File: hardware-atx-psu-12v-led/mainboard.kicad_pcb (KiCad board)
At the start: 2 copper layers, 98 x 103 mm, 100 parts, among them J1 ATX-24, J11 LED, J12 LED, J13 LED, J14 LED, J15 LED, J16 LED, J17 LED, J18 LED, J19 LED, J2 ATX, J20 LED, J21 LED, J22 LED, J23 LED, J24 LED, J25 LED, J26 LED, J27 LED, J28 LED, J29 LED, J3 PA11, J30 LED, J31 LED, J32 LED, J33 LED, J34 LED, J35 LED, J36 LED, J37 LED, J38 LED, J39 LED, J4 PA12, J40 LED, J41 LED, J42 ATX, J43 ATX, J44 ATX, J45 ATX, J5 LED, J6 USB_C_Receptacle_USB2.0, J7 PAGM, J8 PA15, SW1 Download, U1 CH32V305RBT6, U2 AMS1117, Y2 8MHz

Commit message: Tweak holes on power connector
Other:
- board text added: "cnhardware xmastree mainboard rev B"
- board text removed: "cnhardware xmastree mainboard rev A"
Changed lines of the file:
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@@
 			(drillshape 0)
 			(scaleselection 1)
-			(outputdirectory "mainboard-revA/")
+			(outputdirectory "mainboard-revB/")
 		)
 	)
@@
 			(at 0 0.6)
 			(size 2.7 3.3)
-			(drill 1.4)
+			(drill 1.61)
 			(layers "*.Cu" "*.Mask")
 			(remove_unused_layers no)
@@
 			(at 4.2 0.6)
 			(size 2.7 3.3)
-			(drill 1.4)
+			(drill 1.6)
 			(layers "*.Cu" "*.Mask")
 			(remove_unused_layers no)
@@
 			(at 8.4 0.6)
 			(size 2.7 3.3)
-			(drill 1.4)
+			(drill 1.6)
 			(layers "*.Cu" "*.Mask")
 			(remove_unused_layers no)
@@
 			(at 12.6 0.6)
 			(size 2.7 3.3)
-			(drill 1.4)
+			(drill 1.61)
 			(layers "*.Cu" "*.Mask")
 			(remove_unused_layers no)
@@
 			(at 0 4.9)
 			(size 2.7 3.3)
-			(drill 1.4)
+			(drill 1.61)
 			(layers "*.Cu" "*.Mask")
 			(remove_unused_layers no)
@@
 			(at 4.2 4.9)
 			(size 2.7 3.3)
-			(drill 1.4)
+			(drill 1.61)
 			(layers "*.Cu" "*.Mask")
 			(remove_unused_layers no)
@@
 			(at 8.4 4.9)
 			(size 2.7 3.3)
-			(drill 1.4)
+			(drill 1.61)
 			(layers "*.Cu" "*.Mask")
 			(remove_unused_layers no)
@@
 			(at 12.6 4.9)
 			(size 2.7 3.3)
-			(drill 1.4)
+			(drill 1.61)
 			(layers "*.Cu" "*.Mask")
 			(remove_unused_layers no)
@@
 			(at 0 0.6 270)
 			(size 2.7 3.3)
-			(drill 1.4)
+			(drill 1.61)
 			(layers "*.Cu" "*.Mask")
 			(remove_unused_layers no)
@@
 			(at 4.2 0.6 270)
 			(size 2.7 3.3)
-			(drill 1.4)
+			(drill 1.6)
 			(layers "*.Cu" "*.Mask")
 			(remove_unused_layers no)
@@
 			(at 8.4 0.6 270)
 			(size 2.7 3.3)
-			(drill 1.4)
+			(drill 1.6)
 			(layers "*.Cu" "*.Mask")
 			(remove_unused_layers no)
@@
 			(at 12.6 0.6 270)
 			(size 2.7 3.3)
-			(drill 1.4)
+			(drill 1.61)
 			(layers "*.Cu" "*.Mask")
 			(remove_unused_layers no)
@@
 			(at 0 4.9 270)
 			(size 2.7 3.3)
-			(drill 1.4)
+			(drill 1.61)
 			(layers "*.Cu" "*.Mask")
 			(remove_unused_layers no)
@@
 			(at 4.2 4.9 270)
 			(size 2.7 3.3)
-			(drill 1.4)
+			(drill 1.61)
 			(layers "*.Cu" "*.Mask")
 			(remove_unused_layers no)
@@
 			(at 8.4 4.9 270)
 			(size 2.7 3.3)
-			(drill 1.4)
+			(drill 1.61)
 			(layers "*.Cu" "*.Mask")
 			(remove_unused_layers no)
@@
 			(at 12.6 4.9 270)
 			(size 2.7 3.3)
-			(drill 1.4)
+			(drill 1.61)
 			(layers "*.Cu" "*.Mask")
 			(remove_unused_layers no)
@@
 			(at 0 0.6 270)
 			(size 2.7 3.3)
-			(drill 1.4)
+			(drill 1.61)
 			(layers "*.Cu" "*.Mask")
 			(remove_unused_layers no)
@@
 			(at 4.2 0.6 270)
 			(size 2.7 3.3)
-			(drill 1.4)
+			(drill 1.6)
 			(layers "*.Cu" "*.Mask")
 			(remove_unused_layers no)
@@
 			(at 8.4 0.6 270)
 			(size 2.7 3.3)
-			(drill 1.4)
+			(drill 1.6)
 			(layers "*.Cu" "*.Mask")
 			(remove_unused_layers no)
@@
 			(at 12.6 0.6 270)
 			(size 2.7 3.3)
-			(drill 1.4)
+			(drill 1.61)
 			(layers "*.Cu" "*.Mask")
 			(remove_unused_layers no)
@@
 			(at 0 4.9 270)
 			(size 2.7 3.3)
-			(drill 1.4)
+			(drill 1.61)
 			(layers "*.Cu" "*.Mask")
 			(remove_unused_layers no)
@@
 			(at 4.2 4.9 270)
 			(size 2.7 3.3)
-			(drill 1.4)
+			(drill 1.61)
 			(layers "*.Cu" "*.Mask")
 			(remove_unused_layers no)
@@
 			(at 8.4 4.9 270)
 			(size 2.7 3.3)
-			(drill 1.4)
+			(drill 1.61)
 			(layers "*.Cu" "*.Mask")
 			(remove_unused_layers no)
@@
 			(at 12.6 4.9 270)
 			(size 2.7 3.3)
-			(drill 1.4)
+			(drill 1.61)
 			(layers "*.Cu" "*.Mask")
 			(remove_unused_layers no)
@@
 			(at 0 0.6 270)
 			(size 2.7 3.3)
-			(drill 1.4)
+			(drill 1.61)
 			(layers "*.Cu" "*.Mask")
 			(remove_unused_layers no)
@@
 			(at 4.2 0.6 270)
 			(size 2.7 3.3)
-			(drill 1.4)
+			(drill 1.6)
 			(layers "*.Cu" "*.Mask")
 			(remove_unused_layers no)
@@
 			(at 8.4 0.6 270)
 			(size 2.7 3.3)
-			(drill 1.4)
+			(drill 1.6)
 			(layers "*.Cu" "*.Mask")
 			(remove_unused_layers no)
@@
 			(at 12.6 0.6 270)
 			(size 2.7 3.3)
-			(drill 1.4)
+			(drill 1.61)
 			(layers "*.Cu" "*.Mask")
 			(remove_unused_layers no)
@@
 			(at 0 4.9 270)
 			(size 2.7 3.3)
-			(drill 1.4)
+			(drill 1.61)
 			(layers "*.Cu" "*.Mask")
 			(remove_unused_layers no)
@@
 			(at 4.2 4.9 270)
 			(size 2.7 3.3)
-			(drill 1.4)
+			(drill 1.61)
 			(layers "*.Cu" "*.Mask")
 			(remove_unused_layers no)
@@
 			(at 8.4 4.9 270)
 			(size 2.7 3.3)
-			(drill 1.4)
+			(drill 1.61)
 			(layers "*.Cu" "*.Mask")
 			(remove_unused_layers no)
@@
 			(at 12.6 4.9 270)
 			(size 2.7 3.3)
-			(drill 1.4)
+			(drill 1.61)
 			(layers "*.Cu" "*.Mask")
 			(remove_unused_layers no)
@@
 			(at 0 0.6 180)
 			(size 2.7 3.3)
-			(drill 1.4)
+			(drill 1.61)
 			(layers "*.Cu" "*.Mask")
 			(remove_unused_layers no)
@@
 			(at 4.2 0.6 180)
 			(size 2.7 3.3)
-			(drill 1.4)
+			(drill 1.6)
 			(layers "*.Cu" "*.Mask")
 			(remove_unused_layers no)
@@
 			(at 8.4 0.6 180)
 			(size 2.7 3.3)
-			(drill 1.4)
+			(drill 1.6)
 			(layers "*.Cu" "*.Mask")
 			(remove_unused_layers no)
@@
 			(at 12.6 0.6 180)
 			(size 2.7 3.3)
-			(drill 1.4)
+			(drill 1.61)
 			(layers "*.Cu" "*.Mask")
 			(remove_unused_layers no)
@@
 			(at 0 4.9 180)
 			(size 2.7 3.3)
-			(drill 1.4)
+			(drill 1.61)
 			(layers "*.Cu" "*.Mask")
 			(remove_unused_layers no)
@@
 			(at 4.2 4.9 180)
 			(size 2.7 3.3)
-			(drill 1.4)
+			(drill 1.61)
 			(layers "*.Cu" "*.Mask")
 			(remove_unused_layers no)
@@
 			(at 8.4 4.9 180)
 			(size 2.7 3.3)
-			(drill 1.4)
+			(drill 1.61)
 			(layers "*.Cu" "*.Mask")
 			(remove_unused_layers no)
@@
 			(at 12.6 4.9 180)
 			(size 2.7 3.3)
-			(drill 1.4)
+			(drill 1.61)
 			(layers "*.Cu" "*.Mask")
 			(remove_unused_layers no)
@@
 		)
 	)
-	(gr_text "cnhardware\nxmastree\nmainboard\nrev A"
+	(gr_text "cnhardware\nxmastree\nmainboard\nrev B"
 		(at 150.82 59.18 0)
 		(layer "F.SilkS")

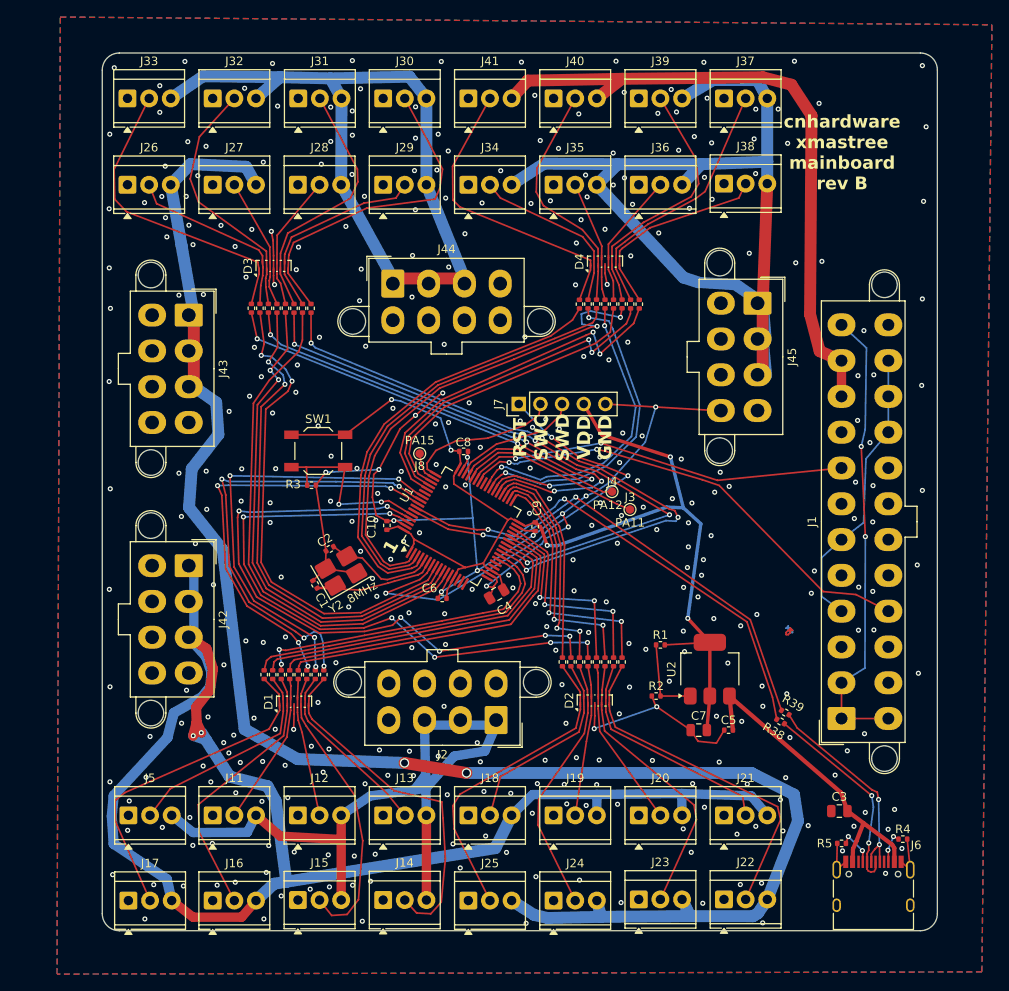
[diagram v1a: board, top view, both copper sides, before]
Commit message: Update with more spacing around connectors
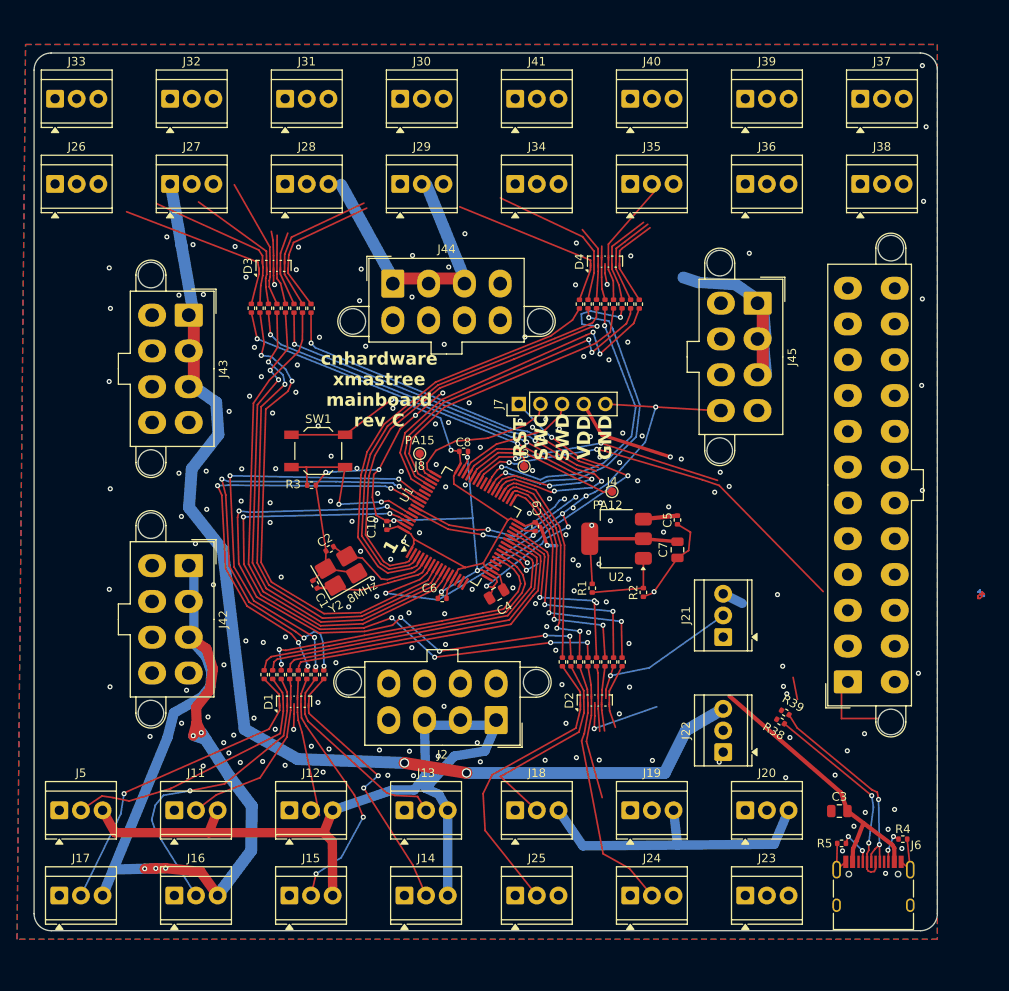
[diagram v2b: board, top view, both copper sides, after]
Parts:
- moved C5 25.4 mm to (131.5, 97.8), turned to 90 degrees
- moved C7 21.3 mm to (131.5, 101.3), turned to 90 degrees
- moved J21 20.9 mm to (136.9, 111.5), turned to 90 degrees
- moved U2 18.8 mm to (124.3, 100.0), turned to 180 degrees
- moved J22 17.3 mm to (136.9, 125.0), turned to 90 degrees
- moved J37 16.0 mm to (153.0, 48.4)
- moved J38 16.0 mm to (153.0, 58.4)
- moved J3 13.4 mm to (113.5, 91.5)
- moved J20 12.5 mm to (139.5, 131.9)
- moved J23 12.5 mm to (139.5, 141.9)
- moved J36 12.5 mm to (139.5, 58.4)
- moved J39 12.5 mm to (139.5, 48.4)
- moved R2 12.3 mm to (127.5, 106.3), turned to 90 degrees
- moved R1 10.4 mm to (121.5, 105.8), turned to 90 degrees
- moved J19 9.02 mm to (126.0, 131.9)
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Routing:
- net 12V5: track 115.2 -> 26.9 mm
- net 12V6: track 76.7 -> 0.00 mm
- net 12V3: track 195.2 -> 129.1 mm
- net 12V4: track 91.6 -> 32.8 mm
- net Net-(J1-+3.3V-Pad1): track 54.6 -> 9.70 mm, vias 2 -> 0
- net VDD: track 140.8 -> 101.2 mm, vias 5 -> 4
- net USBDP: track 57.5 -> 21.2 mm
- net USBDM: track 57.4 -> 22.3 mm
- net Net-(J1-+5V-Pad21): track 33.9 -> 0.00 mm
- net LED12: track 40.6 -> 7.63 mm
- net 12V2: track 169.1 -> 136.7 mm, vias 2 -> 5
- net Net-(U1-PC4): track 74.4 -> 45.7 mm, vias 4 -> 3
- net Net-(U1-PC5): track 73.1 -> 45.4 mm, vias 4 -> 3
- net LED13: track 33.3 -> 7.63 mm
- net LED21: track 30.2 -> 8.81 mm
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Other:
- board size 98 x 103 mm -> 106 x 103 mm
- board text added: "${REFERENCE}"
- board text added: "cnhardware xmastree mainboard rev C"
- board text removed: "cnhardware xmastree mainboard rev B"

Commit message: bump design
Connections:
- J11 pad 3: 12V1 -> 12V2
- J12 pad 3: 12V1 -> 12V2
- J13 pad 3: 12V1 -> 12V2
- J14 pad 3: 12V1 -> 12V2
- J15 pad 3: 12V1 -> 12V2
- J17 pad 3: 12V2 -> 12V3
- J18 pad 3: 12V2 -> 12V1
- J19 pad 3: 12V2 -> 12V1
- J20 pad 3: 12V2 -> 12V1
- J21 pad 3: 12V2 -> 12V6
- J22 pad 3: 12V3 -> 12V6
- J23 pad 3: 12V3 -> 12V1
- J24 pad 3: 12V3 -> 12V1
- J25 pad 3: 12V3 -> 12V1
- J32 pad 3: 12V4 -> 12V3
- J33 pad 3: 12V4 -> 12V3
- J34 pad 3: 12V5 -> 12V4
- J40 pad 3: 12V6 -> 12V5
- J41 pad 3: 12V6 -> 12V4
- J5 pad 3: 12V1 -> 12V3
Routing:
- net 12V5: track 26.9 -> 93.1 mm
- net 12V6: track 0.00 -> 48.9 mm
- net 12V4: track 32.8 -> 80.6 mm
- net 12V2: track 136.7 -> 99.1 mm, vias 5 -> 0
- net 12V1: track 94.8 -> 124.9 mm
- net LED13: track 7.63 -> 36.4 mm, vias 0 -> 1
- net LED10: track 7.66 -> 31.6 mm
- net 12V3: track 129.1 -> 147.3 mm, vias 2 -> 0
- net +5V: track 37.1 -> 19.7 mm
- net LED12: track 7.63 -> 20.3 mm
- net LED9: track 15.8 -> 21.3 mm
- net LED2: track 16.3 -> 15.5 mm
- net GND: vias 197 -> 185
